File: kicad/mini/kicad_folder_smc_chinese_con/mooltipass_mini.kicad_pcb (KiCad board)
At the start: 2 copper layers, 74.9 x 32.5 mm, 65 parts, among them CON1 CON_10118194-0001LF, P1 EMC, P2 EMC, P3 EMC, P4 EMC, Q1 MOS_P, Q2 MOS_N, Q3 MOS_P, Q4 MOS_N, U1 IP4234CZ6,125, U2 ST662ACD, U3 CON_UGM128032A6B01, U4 CON_SMARTCARD2, U5 AT45DB011D, U6 ATMEGA32U4_QFN, U7 LIS2HH12, U8 TS005_WHEEL_CLICK, X1 16MHz

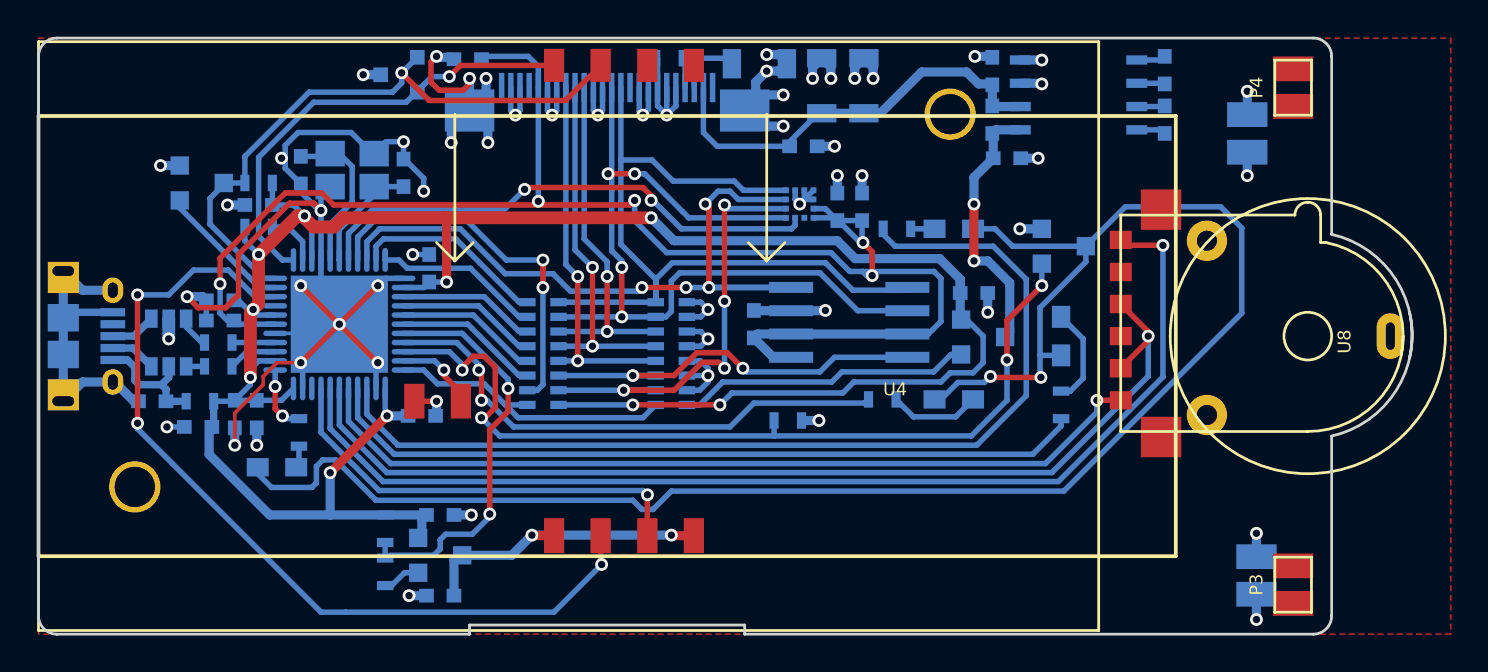
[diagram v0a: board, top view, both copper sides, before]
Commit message: final gerbers for mini with chinese card connector clone
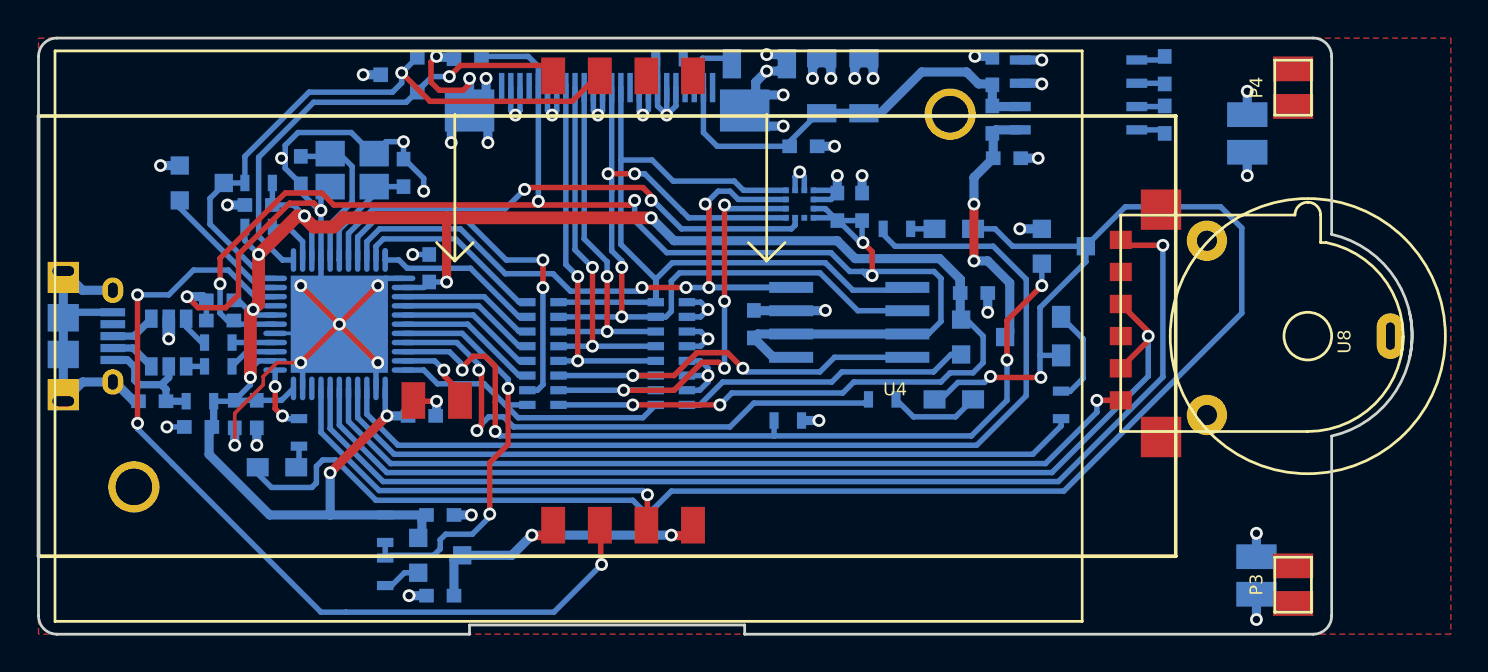
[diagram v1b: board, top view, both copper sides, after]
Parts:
- U4: footprint _kicad4_lib:CON_SMARTCARD_5145300-3 -> _kicad4_lib:CON_SMARTCARD_CLONE_91-90473-003A
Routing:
- net /LED2: track 28.9 -> 30.9 mm
- net GND: track 199.2 -> 200.9 mm
- net /SC_IO: track 34.2 -> 34.9 mm
- net /PWM_LED: track 48.4 -> 47.7 mm
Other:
- board text added: "Mooltipass Mini by Stephan Electronics Licensed under CERN OHL V1.2 v5 - 24/11/2016"
- board text removed: "Mooltipass Mini by Stephan Electronics Licensed under CERN OHL V1.2 v4"
